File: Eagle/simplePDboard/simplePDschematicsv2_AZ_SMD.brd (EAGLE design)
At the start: 28 x 28 mm, 16 parts, among them IC1 OP27Z

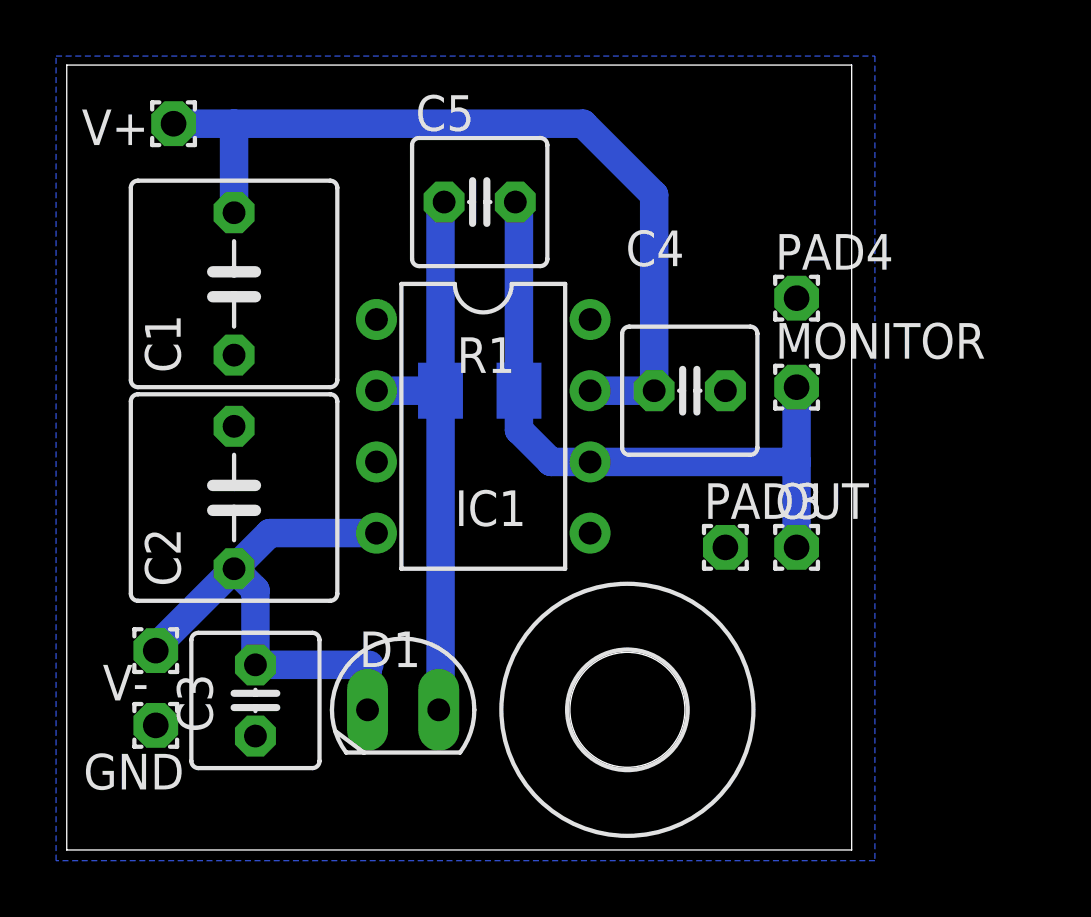
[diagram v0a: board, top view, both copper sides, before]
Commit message: updated the PD board. PD was always properly connected. Now the symbol corresponds also to the PD we have.
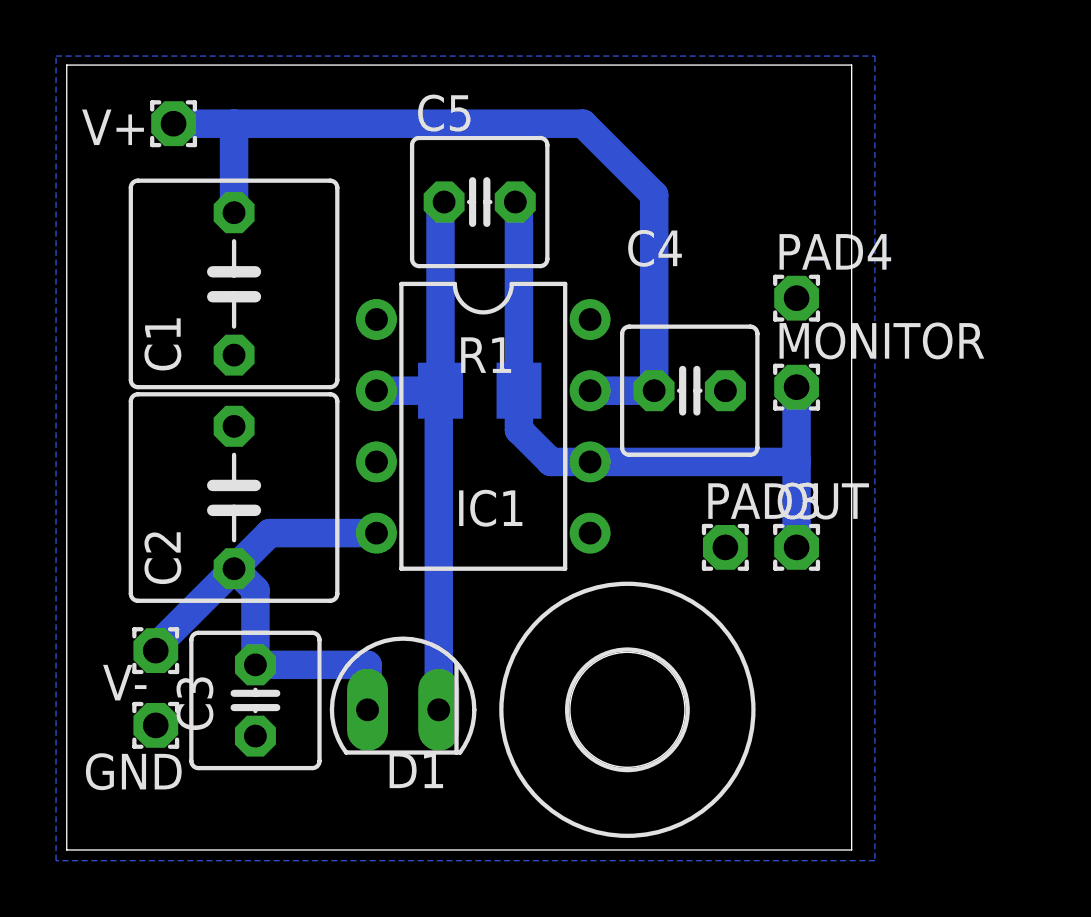
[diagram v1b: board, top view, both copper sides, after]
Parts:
- D1: value SFH205 -> SFH206; device opto-trans-siemens:SFH205 -> opto-trans-siemens:SFH206
- turned D1 to 270 degrees
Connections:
- removed net N$1: C5.1, D1.A, IC1.2, R1.1
- new net N$3: C5.1, D1.K, IC1.2, R1.1
- net V-: now also D1.A; no longer D1.K
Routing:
- net N$3: track 0.00 -> 20.5 mm
- net N$1: track 20.1 -> 0.00 mm
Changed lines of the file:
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@@
 <wire x1="0" y1="28" x2="0" y2="0" width="0" layer="20"/>
 <dimension x1="0" y1="28" x2="0" y2="0" x3="-5.08" y3="14" textsize="1.778" layer="47"/>
-<dimension x1="27.84" y1="28" x2="0" y2="28" x3="13.92" y3="31.877" textsize="1.778" layer="47"/>
+<dimension x1="0" y1="28" x2="28" y2="28" x3="14" y3="29.845" textsize="1.778" layer="47"/>
 </plain>
 <attributes>
@@
 <attribute name="VALUE" x="14.986" y="25.654" size="1.27" layer="27" ratio="10"/>
 </element>
-<element name="D1" library="opto-trans-siemens" package="SFH205" value="SFH205" x="12" y="5" smashed="yes" rot="R90">
-<attribute name="OC_NEWARK" value="unknown" x="12" y="5" size="1.778" layer="27" rot="R90" display="off"/>
-<attribute name="MF" value="" x="12" y="5" size="1.778" layer="27" rot="R90" display="off"/>
-<attribute name="OC_FARNELL" value="unknown" x="12" y="5" size="1.778" layer="27" rot="R90" display="off"/>
-<attribute name="MPN" value="" x="12" y="5" size="1.778" layer="27" rot="R90" display="off"/>
-<attribute name="NAME" x="12.635" y="7.794" size="1.27" layer="25" ratio="10" rot="R180"/>
-<attribute name="VALUE" x="15.81" y="9.191" size="1.27" layer="27" ratio="10" rot="R180"/>
+<element name="D1" library="opto-trans-siemens" package="SFH206" value="SFH206" x="12" y="5" smashed="yes" rot="R270">
+<attribute name="OC_NEWARK" value="01M8807" x="12" y="5" size="1.778" layer="27" rot="R270" display="off"/>
+<attribute name="MF" value="" x="12" y="5" size="1.778" layer="27" rot="R270" display="off"/>
+<attribute name="OC_FARNELL" value="1212741" x="12" y="5" size="1.778" layer="27" rot="R270" display="off"/>
+<attribute name="MPN" value="SFH206K" x="12" y="5" size="1.778" layer="27" rot="R270" display="off"/>
+<attribute name="NAME" x="11.365" y="2.206" size="1.27" layer="25" ratio="10"/>
+<attribute name="VALUE" x="8.19" y="0.809" size="1.27" layer="27" ratio="10"/>
 </element>
 <element name="IC1" library="linear" package="DIL08" value="OP27Z" x="14.859" y="15.113" smashed="yes" rot="R270">
@@
 <wire x1="26.035" y1="16.51" x2="26.035" y2="13.843" width="1.016" layer="16"/>
 </signal>
-<signal name="N$1">
-<contactref element="IC1" pad="2"/>
-<contactref element="R1" pad="1"/>
-<contactref element="C5" pad="1"/>
-<wire x1="13.332" y1="16.383" x2="11.049" y2="16.383" width="1.016" layer="16"/>
-<wire x1="13.462" y1="23.114" x2="13.332" y2="22.984" width="1.016" layer="16"/>
-<wire x1="13.332" y1="22.984" x2="13.332" y2="16.383" width="1.016" layer="16"/>
-<wire x1="13.27" y1="16.383" x2="13.332" y2="16.383" width="1.016" layer="16"/>
-<contactref element="D1" pad="A"/>
-<wire x1="13.27" y1="5" x2="13.335" y2="5" width="1.016" layer="16"/>
-<wire x1="13.335" y1="5" x2="13.335" y2="15.875" width="1.016" layer="16"/>
-<wire x1="13.335" y1="15.875" x2="13.332" y2="16.383" width="0" layer="19" extent="16-16"/>
-</signal>
 <signal name="V+">
 <contactref element="C1" pad="2"/>
@@
 <wire x1="6.731" y1="6.604" x2="6.731" y2="9.271" width="1.016" layer="16"/>
 <wire x1="6.731" y1="9.271" x2="5.969" y2="10.033" width="1.016" layer="16"/>
+<contactref element="D1" pad="A"/>
+<wire x1="6.731" y1="6.604" x2="10.73" y2="6.604" width="1.016" layer="16"/>
+<wire x1="10.73" y1="6.604" x2="10.73" y2="5" width="1.016" layer="16"/>
+</signal>
+<signal name="N$3">
 <contactref element="D1" pad="K"/>
-<wire x1="6.731" y1="6.604" x2="10.795" y2="6.604" width="1.016" layer="16"/>
-<wire x1="10.795" y1="6.604" x2="10.795" y2="6.35" width="0.4064" layer="16"/>
-<wire x1="10.795" y1="6.35" x2="10.73" y2="6.35" width="0.4064" layer="16"/>
-<wire x1="10.73" y1="6.35" x2="10.73" y2="5" width="1.016" layer="16"/>
+<contactref element="IC1" pad="2"/>
+<contactref element="R1" pad="1"/>
+<contactref element="C5" pad="1"/>
+<wire x1="13.332" y1="16.383" x2="11.049" y2="16.383" width="1.016" layer="16"/>
+<wire x1="13.462" y1="23.114" x2="13.332" y2="22.984" width="1.016" layer="16"/>
+<wire x1="13.332" y1="22.984" x2="13.332" y2="16.383" width="1.016" layer="16"/>
+<wire x1="13.332" y1="16.383" x2="13.27" y2="16.383" width="1.016" layer="16"/>
+<wire x1="13.27" y1="16.383" x2="13.27" y2="5" width="1.016" layer="16"/>
 </signal>
 </signals>

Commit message: replaced the OP27 by a TL071 in the TI circuit
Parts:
- IC1: value OP27Z -> TL071P
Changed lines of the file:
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@@
 <attribute name="VALUE" x="8.19" y="0.809" size="1.27" layer="27" ratio="10"/>
 </element>
-<element name="IC1" library="linear" package="DIL08" value="OP27Z" x="14.859" y="15.113" smashed="yes" rot="R270">
+<element name="IC1" library="linear" package="DIL08" value="TL071P" x="14.859" y="15.113" smashed="yes" rot="R270">
 <attribute name="NAME" x="13.843" y="11.557" size="1.27" layer="25" ratio="10"/>
 <attribute name="VALUE" x="10.668" y="8.128" size="1.27" layer="27" ratio="10"/>
